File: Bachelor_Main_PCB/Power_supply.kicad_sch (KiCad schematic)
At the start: 0 parts

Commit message: Started on PSU sheet
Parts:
- added C44: 47uF, Capacitor_SMD:C_0603_1608Metric, symbol Device:C_Small
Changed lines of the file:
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@@
 	(generator_version "9.0")
 	(paper "A4")
+	(global_label "V_IN"
+		(shape input)
+		(at 27.94 25.4 180)
+		(fields_autoplaced yes)
+		(effects
+			(font
+				(size 1.27 1.27)
+			)
+			(justify right)
+		)
+		(property "Intersheetrefs" "${INTERSHEET_REFS}"
+			(at 20.9633 25.4 0)
+			(effects
+				(font
+					(size 1.27 1.27)
+				)
+				(justify right)
+				(hide yes)
+			)
+		)
+	)
+	(symbol
+		(lib_id "Device:C_Small")
+		(at 36.83 27.94 0)
+		(unit 1)
+		(exclude_from_sim no)
+		(in_bom yes)
+		(on_board yes)
+		(dnp no)
+		(property "Reference" "C44"
+			(at 34.036 27.94 90)
+			(effects
+				(font
+					(size 1.27 1.27)
+				)
+			)
+		)
+		(property "Value" "47uF"
+			(at 39.37 27.432 90)
+			(effects
+				(font
+					(size 1.27 1.27)
+				)
+			)
+		)
+		(property "Footprint" "Capacitor_SMD:C_0603_1608Metric"
+			(at 36.83 27.94 0)
+			(effects
+				(font
+					(size 1.27 1.27)
+				)
+				(hide yes)
+			)
+		)
+		(property "Datasheet" "~"
+			(at 36.83 27.94 0)
+			(effects
+				(font
+					(size 1.27 1.27)
+				)
+				(hide yes)
+			)
+		)
+		(property "Description" "Unpolarized capacitor, small symbol"
+			(at 36.83 27.94 0)
+			(effects
+				(font
+					(size 1.27 1.27)
+				)
+				(hide yes)
+			)
+		)
+		(property "Field5" ""
+			(at 36.83 27.94 0)
+			(effects
+				(font
+					(size 1.27 1.27)
+				)
+				(hide yes)
+			)
+		)
+		(property "Field6" ""
+			(at 36.83 27.94 0)
+			(effects
+				(font
+					(size 1.27 1.27)
+				)
+				(hide yes)
+			)
+		)
+		(pin "2"
+		)
+		(pin "1"
+		)
+		(instances
+			(project "Bachelor_Main_PCB"
+				(path "/3544d663-329e-4884-b753-28436ca187e8/4408de3e-a395-4433-a2e1-ccefac59f96e"
+					(reference "C44")
+					(unit 1)
+				)
+			)
+		)
+	)
 )

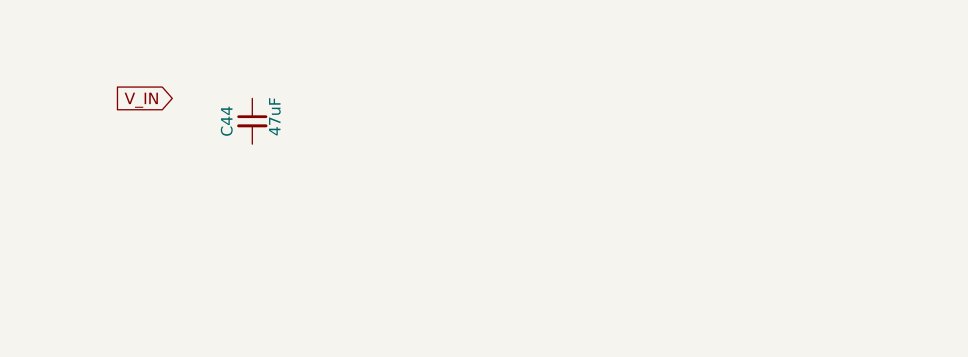
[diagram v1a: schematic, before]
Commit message: add LM 73100 ideal diode
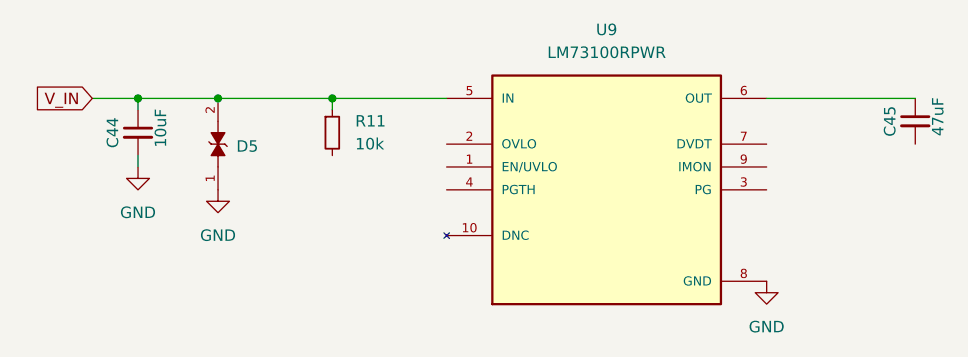
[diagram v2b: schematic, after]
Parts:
- added C45: 47uF, Capacitor_SMD:C_0603_1608Metric, symbol Device:C_Small
- added D5: 0402ESDA-MLP1, 0402ESDA-MLP1:ESD_0402ESDA-MLP1, symbol 0402ESDA-MLP1:0402ESDA-MLP1
- added R11: 10k, Resistor_SMD:R_0402_1005Metric, symbol Device:R_Small
- added U9: LM73100RPWR, LM73100RPWR:IC_LM73100RPWR, symbol LM73100RPWR:LM73100RPWR
- C44: value 47uF -> 10uF
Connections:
- net V_IN: now also C44.1, D5.2, R11.1, U9.5 (IN)
- net GND: now reaches C44.2
- net GND: now also D5.1, U9.8 (GND)
- new net: C45.1, U9.6 (OUT)
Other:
- moved on the sheet: C44

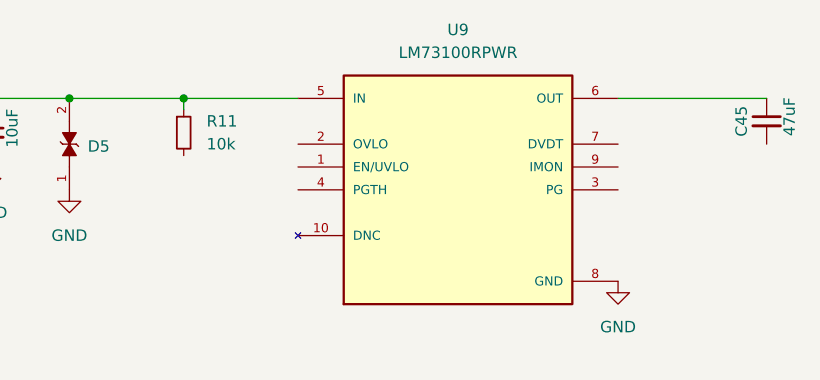
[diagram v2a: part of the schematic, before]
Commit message: Added RIMON + R1,R2,R3 to Ideal diode circuit
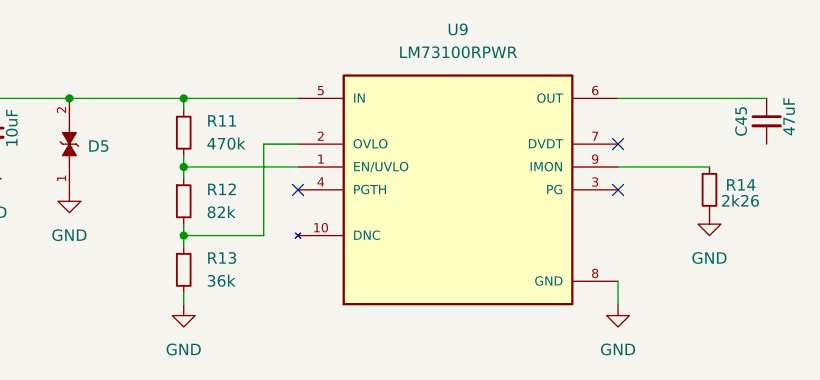
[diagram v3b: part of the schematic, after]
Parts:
- added R12: 82k, Resistor_SMD:R_0402_1005Metric, symbol Device:R_Small
- added R13: 36k, Resistor_SMD:R_0402_1005Metric, symbol Device:R_Small
- added R14: 2k26, Resistor_SMD:R_0402_1005Metric, symbol Device:R_Small
- R11: value 10k -> 470k
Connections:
- net GND: now also R13.2, R14.2
- net at R11.2: now also U9.1 (EN/UVLO), R12.1
- net at U9.2 (OVLO): now also R12.2, R13.1
- net at U9.9 (IMON): now also R14.1
- no-connect marks 0 -> 3

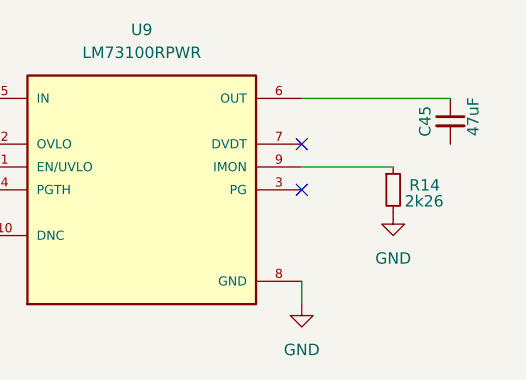
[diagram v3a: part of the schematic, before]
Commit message: Add RPI to MCU UART communication
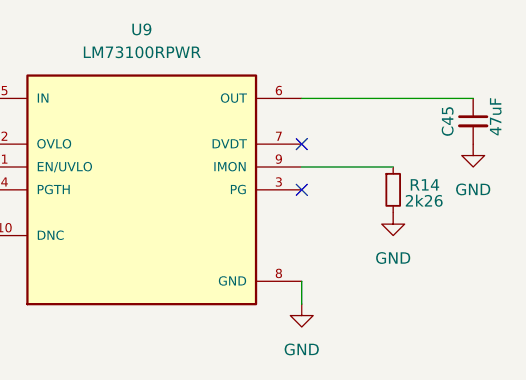
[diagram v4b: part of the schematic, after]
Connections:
- net GND: now also C45.2
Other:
- moved on the sheet: C45
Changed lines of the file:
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@@
 	(wire
 		(pts
-			(xy 93.98 25.4) (xy 110.49 25.4)
+			(xy 93.98 25.4) (xy 113.03 25.4)
 		)
 		(stroke
@@
 	(symbol
 		(lib_id "Device:C_Small")
-		(at 110.49 27.94 0)
+		(at 113.03 27.94 0)
 		(unit 1)
 		(exclude_from_sim no)
@@
 		(dnp no)
 		(property "Reference" "C45"
-			(at 107.696 27.94 90)
+			(at 110.236 27.94 90)
 			(effects
 				(font
@@
 		)
 		(property "Value" "47uF"
-			(at 113.03 27.432 90)
+			(at 115.57 27.432 90)
 			(effects
 				(font
@@
 		)
 		(property "Footprint" "Capacitor_SMD:C_0603_1608Metric"
-			(at 110.49 27.94 0)
+			(at 113.03 27.94 0)
 			(effects
 				(font
@@
 		)
 		(property "Datasheet" "~"
-			(at 110.49 27.94 0)
+			(at 113.03 27.94 0)
 			(effects
 				(font
@@
 		)
 		(property "Description" "Unpolarized capacitor, small symbol"
-			(at 110.49 27.94 0)
+			(at 113.03 27.94 0)
 			(effects
 				(font
@@
 		)
 		(property "Field5" ""
-			(at 110.49 27.94 0)
+			(at 113.03 27.94 0)
 			(effects
 				(font
@@
 		)
 		(property "Field6" ""
-			(at 110.49 27.94 0)
+			(at 113.03 27.94 0)
 			(effects
 				(font
@@
 					(unit 1)
 				)
+			)
+		)
+	)
+	(symbol
+		(lib_id "power:GND")
+		(at 113.03 30.48 0)
+		(unit 1)
+		(exclude_from_sim no)
+		(in_bom yes)
+		(on_board yes)
+		(dnp no)
+		(fields_autoplaced yes)
+		(property "Reference" "#PWR050"
+			(at 113.03 36.83 0)
+			(effects
+				(font
+					(size 1.27 1.27)
+				)
+				(hide yes)
+			)
+		)
+		(property "Value" "GND"
+			(at 113.03 35.56 0)
+			(effects
+				(font
+					(size 1.27 1.27)
+				)
+			)
+		)
+		(property "Footprint" ""
+			(at 113.03 30.48 0)
+			(effects
+				(font
+					(size 1.27 1.27)
+				)
+				(hide yes)
+			)
+		)
+		(property "Datasheet" ""
+			(at 113.03 30.48 0)
+			(effects
+				(font
+					(size 1.27 1.27)
+				)
+				(hide yes)
+			)
+		)
+		(property "Description" "Power symbol creates a global label with name \"GND\" , ground"
+			(at 113.03 30.48 0)
+			(effects
+				(font
+					(size 1.27 1.27)
+				)
+				(hide yes)
+			)
+		)
+		(pin "1"
+		)
+		(instances
+			(project "Bachelor_Main_PCB"
+				(path "/3544d663-329e-4884-b753-28436ca187e8/4408de3e-a395-4433-a2e1-ccefac59f96e"
+					(reference "#PWR050")
+					(unit 1)
+				)

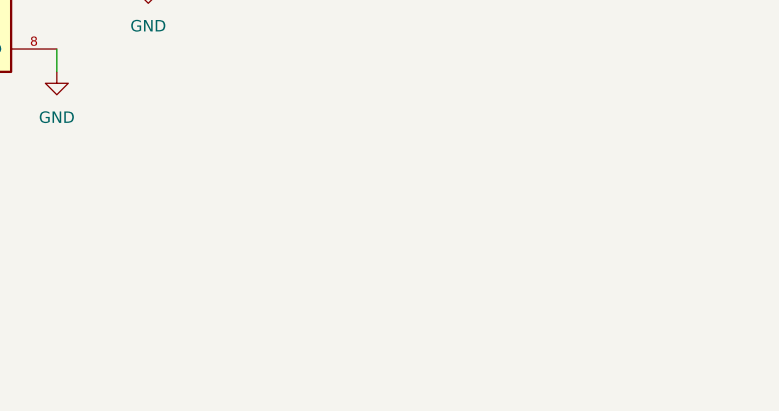
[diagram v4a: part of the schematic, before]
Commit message: Add 1,8v regulator
LD3985M18R
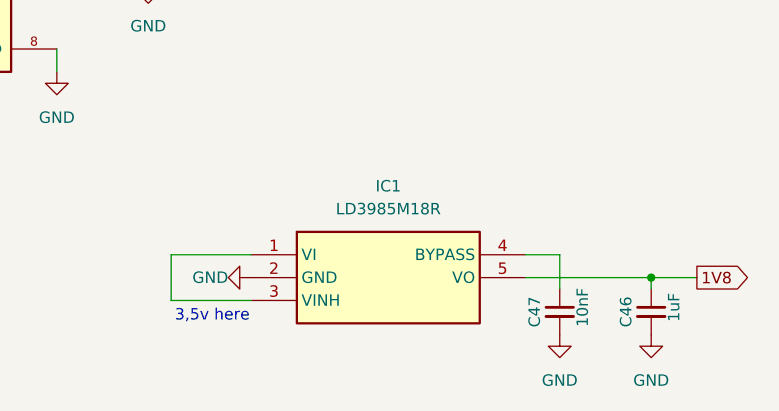
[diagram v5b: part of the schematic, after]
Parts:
- added C46: 1uF, Capacitor_SMD:C_0603_1608Metric, symbol Device:C_Small
- added C47: 10nF, Capacitor_SMD:C_0603_1608Metric, symbol Device:C_Small
- added IC1: LD3985M18R, SOT95P280X145-5N, symbol LD3985M18R:LD3985M18R
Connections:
- net GND: now also C46.2, C47.2, IC1.2 (GND)
- new net: C47.1, IC1.4 (BYPASS)
- new net: IC1.1 (VI), IC1.3 (VINH)
- new net 1V8: C46.1, IC1.5 (VO)
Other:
- note added: "3,5v here"

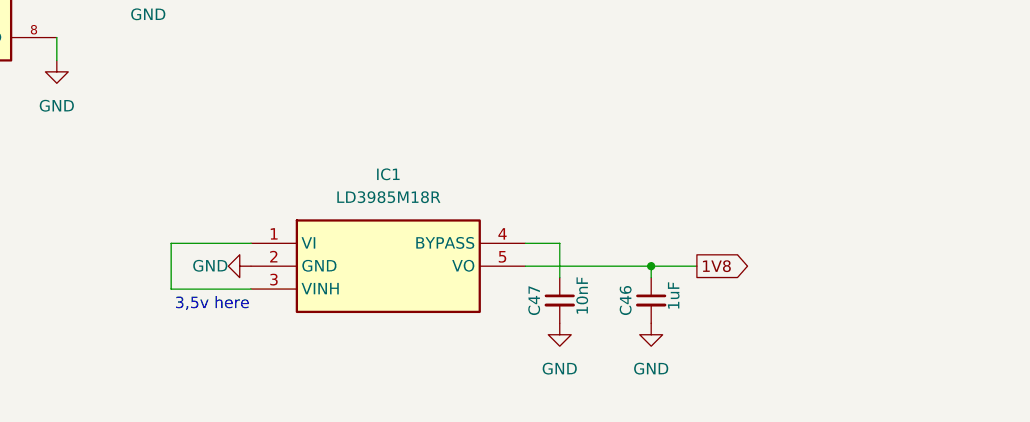
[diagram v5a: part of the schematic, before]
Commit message: updated 1,8v global lables
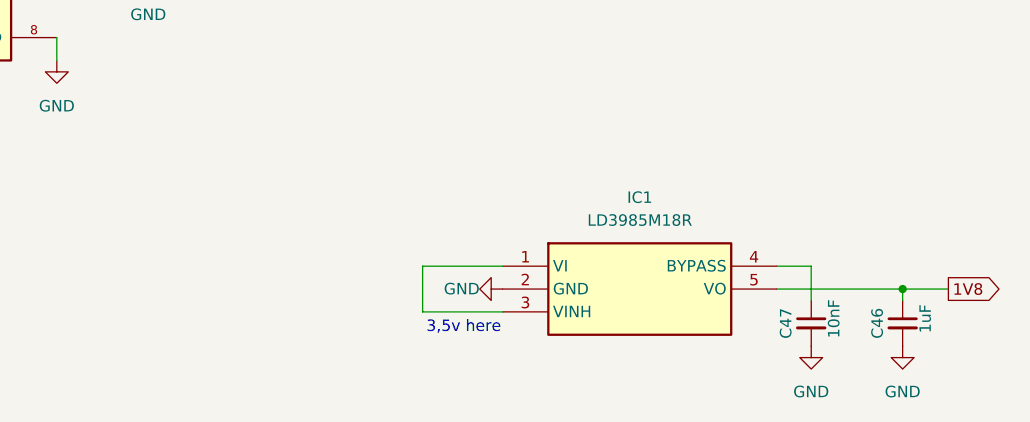
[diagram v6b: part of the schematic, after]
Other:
- moved on the sheet: C46, C47, IC1
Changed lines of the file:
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@@
 	(text "3,5v here"
 		(exclude_from_sim no)
-		(at 111.252 75.438 0)
+		(at 139.192 77.978 0)
 		(effects
 			(font
@@
 	)
 	(junction
-		(at 160.02 71.12)
+		(at 187.96 73.66)
 		(diameter 0)
 		(color 0 0 0 0)
@@
 	(wire
 		(pts
-			(xy 165.1 71.12) (xy 160.02 71.12)
+			(xy 193.04 73.66) (xy 187.96 73.66)
 		)
 		(stroke
@@
 	(wire
 		(pts
-			(xy 160.02 72.39) (xy 160.02 71.12)
+			(xy 187.96 74.93) (xy 187.96 73.66)
 		)
 		(stroke
@@
 	(wire
 		(pts
-			(xy 115.57 73.66) (xy 106.68 73.66)
+			(xy 143.51 76.2) (xy 134.62 76.2)
 		)
 		(stroke
@@
 	(wire
 		(pts
-			(xy 106.68 73.66) (xy 106.68 68.58)
-		)
-		(stroke
-			(width 0)
-			(type default)
-		)
-	)
-	(wire
-		(pts
-			(xy 149.86 68.58) (xy 146.05 68.58)
-		)
-		(stroke
-			(width 0)
-			(type default)
-		)
-	)
-	(wire
-		(pts
-			(xy 106.68 68.58) (xy 115.57 68.58)
-		)
-		(stroke
-			(width 0)
-			(type default)
-		)
-	)
-	(wire
-		(pts
-			(xy 149.86 72.39) (xy 149.86 68.58)
+			(xy 134.62 76.2) (xy 134.62 71.12)
+		)
+		(stroke
+			(width 0)
+			(type default)
+		)
+	)
+	(wire
+		(pts
+			(xy 177.8 71.12) (xy 173.99 71.12)
+		)
+		(stroke
+			(width 0)
+			(type default)
+		)
+	)
+	(wire
+		(pts
+			(xy 134.62 71.12) (xy 143.51 71.12)
+		)
+		(stroke
+			(width 0)
+			(type default)
+		)
+	)
+	(wire
+		(pts
+			(xy 177.8 74.93) (xy 177.8 71.12)
 		)
 		(stroke
@@
 	(wire
 		(pts
-			(xy 146.05 71.12) (xy 160.02 71.12)
+			(xy 173.99 73.66) (xy 187.96 73.66)
 		)
 		(stroke
@@
 	(global_label "1V8"
 		(shape output)
-		(at 165.1 71.12 0)
+		(at 193.04 73.66 0)
 		(fields_autoplaced yes)
 		(effects
@@
 		)
 		(property "Intersheetrefs" "${INTERSHEET_REFS}"
-			(at 171.5928 71.12 0)
+			(at 199.5328 73.66 0)
 			(effects
 				(font
@@
 	(symbol
 		(lib_id "Device:C_Small")
-		(at 160.02 74.93 0)
+		(at 187.96 77.47 0)
 		(unit 1)
 		(exclude_from_sim no)
@@
 		(dnp no)
 		(property "Reference" "C46"
-			(at 157.226 74.93 90)
+			(at 185.166 77.47 90)
 			(effects
 				(font
@@
 		)
 		(property "Value" "1uF"
-			(at 162.56 74.422 90)
+			(at 190.5 76.962 90)
 			(effects
 				(font
@@
 		)
 		(property "Footprint" "Capacitor_SMD:C_0603_1608Metric"
-			(at 160.02 74.93 0)
+			(at 187.96 77.47 0)
 			(effects
 				(font
@@
 		)
 		(property "Datasheet" "~"
-			(at 160.02 74.93 0)
+			(at 187.96 77.47 0)
 			(effects
 				(font
@@
 		)
 		(property "Description" "Unpolarized capacitor, small symbol"
-			(at 160.02 74.93 0)
+			(at 187.96 77.47 0)
 			(effects
 				(font
@@
 		)
 		(property "Field5" ""
-			(at 160.02 74.93 0)
+			(at 187.96 77.47 0)
 			(effects
 				(font
@@
 		)
 		(property "Field6" ""
-			(at 160.02 74.93 0)
+			(at 187.96 77.47 0)
 			(effects
 				(font
@@
 	(symbol
 		(lib_id "power:GND")
-		(at 115.57 71.12 270)
+		(at 143.51 73.66 270)
 		(unit 1)
 		(exclude_from_sim no)
@@
 		(dnp no)
 		(property "Reference" "#PWR051"
-			(at 109.22 71.12 0)
+			(at 137.16 73.66 0)
 			(effects
 				(font
@@
 		)
 		(property "Value" "GND"
-			(at 113.03 71.12 90)
+			(at 140.97 73.66 90)
 			(effects
 				(font
@@
 		)
 		(property "Footprint" ""
-			(at 115.57 71.12 0)
+			(at 143.51 73.66 0)
 			(effects
 				(font
@@
 		)
 		(property "Datasheet" ""
-			(at 115.57 71.12 0)
+			(at 143.51 73.66 0)
 			(effects
 				(font
@@
 		)
 		(property "Description" "Power symbol creates a global label with name \"GND\" , ground"
-			(at 115.57 71.12 0)
+			(at 143.51 73.66 0)
 			(effects
 				(font
@@
 	(symbol
 		(lib_id "power:GND")
-		(at 149.86 77.47 0)
+		(at 177.8 80.01 0)
 		(unit 1)
 		(exclude_from_sim no)
@@
 		(fields_autoplaced yes)
 		(property "Reference" "#PWR053"
-			(at 149.86 83.82 0)
+			(at 177.8 86.36 0)
 			(effects
 				(font
@@
 		)
 		(property "Value" "GND"
-			(at 149.86 82.55 0)
+			(at 177.8 85.09 0)
 			(effects
 				(font
@@
 		)
 		(property "Footprint" ""
-			(at 149.86 77.47 0)
+			(at 177.8 80.01 0)
 			(effects
 				(font
@@
 		)
 		(property "Datasheet" ""
-			(at 149.86 77.47 0)
+			(at 177.8 80.01 0)
 			(effects
 				(font
@@
 		)
 		(property "Description" "Power symbol creates a global label with name \"GND\" , ground"
-			(at 149.86 77.47 0)
+			(at 177.8 80.01 0)
 			(effects
 				(font
@@
 	(symbol
 		(lib_id "Device:C_Small")
-		(at 149.86 74.93 0)
+		(at 177.8 77.47 0)
 		(unit 1)
 		(exclude_from_sim no)
@@
 		(dnp no)
 		(property "Reference" "C47"
-			(at 147.066 74.93 90)
+			(at 175.006 77.47 90)
 			(effects
 				(font
@@
 		)
 		(property "Value" "10nF"
-			(at 152.4 74.422 90)
+			(at 180.34 76.962 90)
 			(effects
 				(font
@@
 		)
 		(property "Footprint" "Capacitor_SMD:C_0603_1608Metric"
-			(at 149.86 74.93 0)
+			(at 177.8 77.47 0)
 			(effects
 				(font
@@
 		)
 		(property "Datasheet" "~"
-			(at 149.86 74.93 0)
+			(at 177.8 77.47 0)
 			(effects
 				(font
@@
 		)
 		(property "Description" "Unpolarized capacitor, small symbol"
-			(at 149.86 74.93 0)
+			(at 177.8 77.47 0)
 			(effects
 				(font
@@
 		)
 		(property "Field5" ""
-			(at 149.86 74.93 0)
+			(at 177.8 77.47 0)
 			(effects
 				(font
@@
 		)
 		(property "Field6" ""
-			(at 149.86 74.93 0)
+			(at 177.8 77.47 0)
 			(effects
 				(font
@@
 	(symbol
 		(lib_id "power:GND")
-		(at 160.02 77.47 0)
+		(at 187.96 80.01 0)
 		(unit 1)
 		(exclude_from_sim no)
@@
 		(fields_autoplaced yes)
 		(property "Reference" "#PWR052"
-			(at 160.02 83.82 0)
+			(at 187.96 86.36 0)
 			(effects
 				(font
@@
 		)
 		(property "Value" "GND"
-			(at 160.02 82.55 0)
+			(at 187.96 85.09 0)
 			(effects
 				(font
@@
 		)
 		(property "Footprint" ""
-			(at 160.02 77.47 0)
+			(at 187.96 80.01 0)
 			(effects
 				(font
@@
 		)
 		(property "Datasheet" ""
-			(at 160.02 77.47 0)
+			(at 187.96 80.01 0)
 			(effects
 				(font
@@
 		)
 		(property "Description" "Power symbol creates a global label with name \"GND\" , ground"
-			(at 160.02 77.47 0)
+			(at 187.96 80.01 0)
 			(effects
 				(font
@@
 	(symbol
 		(lib_id "LD3985M18R:LD3985M18R")
-		(at 115.57 68.58 0)
+		(at 143.51 71.12 0)
 		(unit 1)
 		(exclude_from_sim no)
@@
 		(fields_autoplaced yes)
 		(property "Reference" "IC1"
-			(at 130.81 60.96 0)
+			(at 158.75 63.5 0)
 			(effects
 				(font
@@
 		)
 		(property "Value" "LD3985M18R"
-			(at 130.81 63.5 0)
+			(at 158.75 66.04 0)
 			(effects
 				(font
@@
 		)
 		(property "Footprint" "SOT95P280X145-5N"
-			(at 142.24 163.5 0)
+			(at 170.18 166.04 0)
 			(effects
 				(font
@@
 		)
 		(property "Datasheet" "http://www.st.com/st-web-ui/static/active/en/resource/technical/document/datasheet/CD00003395.pdf"
-			(at 142.24 263.5 0)
+			(at 170.18 266.04 0)
 			(effects
 				(font
@@
 		)
 		(property "Description" "LD3985M18R, Low Dropout Voltage Regulator, 0.55A, 1.8 V +/-3%, 2.5  6 Vin, 5-Pin SOT-23"
-			(at 115.57 68.58 0)
+			(at 143.51 71.12 0)
 			(effects
 				(font
@@
 		)
 		(property "Height" "1.45"
-			(at 142.24 463.5 0)
+			(at 170.18 466.04 0)
 			(effects
 				(font
@@
 		)
 		(property "Manufacturer_Name" "STMicroelectronics"
-			(at 142.24 563.5 0)
+			(at 170.18 566.04 0)
 			(effects
 				(font
@@
 		)
 		(property "Manufacturer_Part_Number" "LD3985M18R"
-			(at 142.24 663.5 0)
+			(at 170.18 666.04 0)
 			(effects
 				(font
@@
 		)
 		(property "Mouser Part Number" "511-LD3985M18R"
-			(at 142.24 763.5 0)
+			(at 170.18 766.04 0)
 			(effects
 				(font
@@
 		)
 		(property "Mouser Price/Stock" "https://www.mouser.co.uk/ProductDetail/STMicroelectronics/LD3985M18R?qs=xaanzPuKu%252BCT%252BZrNaSjvng%3D%3D"
-			(at 142.24 863.5 0)
+			(at 170.18 866.04 0)
 			(effects
 				(font
@@
 		)
 		(property "Arrow Part Number" "LD3985M18R"
-			(at 142.24 963.5 0)
+			(at 170.18 966.04 0)
 			(effects
 				(font
@@
 		)
 		(property "Arrow Price/Stock" "https://www.arrow.com/en/products/ld3985m18r/stmicroelectronics?region=nac"
-			(at 142.24 1063.5 0)
-			(effects
-				(font
+			(at 170.18 1066.04 0)
+			(effects
+				(font
